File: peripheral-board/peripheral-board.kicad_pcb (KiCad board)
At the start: 2 copper layers, 165 x 100 mm, 248 parts, among them CON4001 BARREL_JACK, CON8001 SD_Card, J4001 53047-0510, J7001 FCR1295, J7002 53047-0310, P1001 Peripheral Bus, P1002 Power, Q4001 IRLML2244TRPbF, Q8001 BSS84LT1G, SW1001 Power, SW2001 1, SW2002 2, SW2003 3, SW2004 4, SW2005 5, SW2006 6, SW2007 7, SW2008 8, SW2009 9, SW2010 0, SW2011 +, SW2012 ´, SW2013 BKSP, SW2014 TROLL, SW2015 §, SW2016 UP, SW2017 RMB, SW2018 Q, SW2019 W, SW2020 E, SW2021 R, SW2022 T, SW2023 Y, SW2024 U, SW2025 I, SW2026 O, SW2027 P, SW2028 Å, SW2029 ¨, SW2030 RETURN, SW2031 ALT_GR, SW2032 <, SW2033 LEFT, SW2034 MMB, SW2035 A, SW2036 S, SW2037 D, SW2038 F, SW2039 G, SW2040 H, SW2041 J, SW2042 K, SW2043 L, SW2044 Ö, SW2045 Ä, SW2046 ', SW2047 ESC, SW2048 TAB, SW2049 ALT, SW2050 DOWN, SW2051 LMB, SW2052 SHIFT_L, SW2053 Z, SW2054 X, SW2055 C, SW2056 V, SW2057 B, SW2058 N, SW2059 M, SW2060 ,, SW2061 ., SW2062 -, SW2063 SHIFT_R, SW2064 FN_R, SW2065 SPACE, SW2066 FN_L, SW2067 RIGHT, SW2068 CTRL, SW2069 SPACE, U1001 ATTINY48-A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

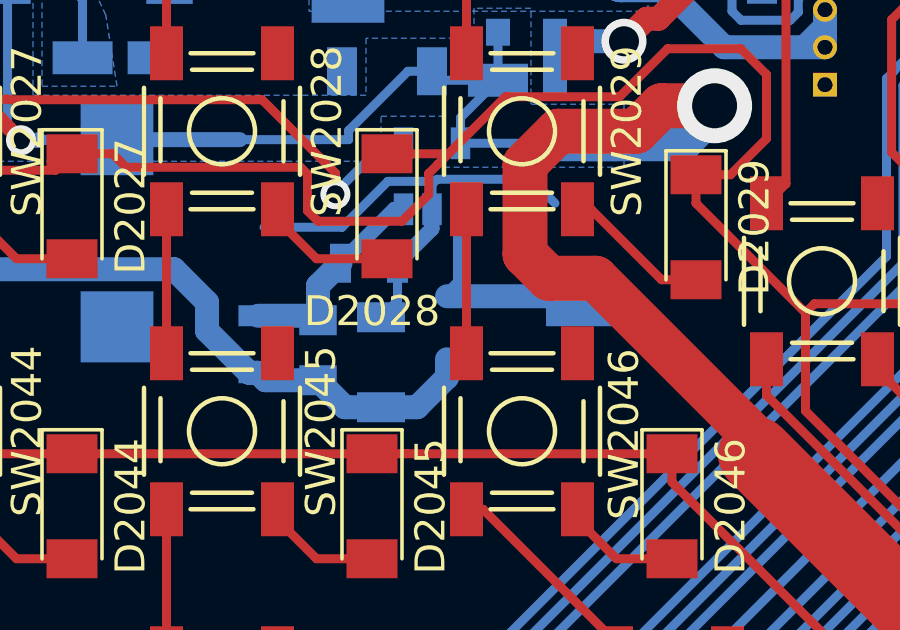
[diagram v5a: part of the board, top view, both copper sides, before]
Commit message: moved power supply capacitor to accomodate larger battery
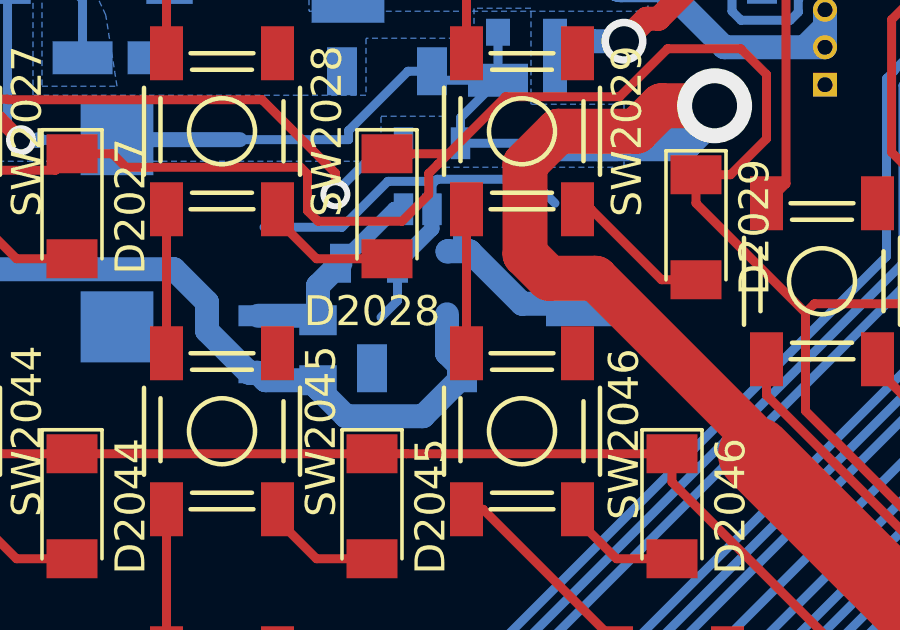
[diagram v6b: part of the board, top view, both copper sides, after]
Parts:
- moved D4007 1.50 mm to (215.0, 75.0)
- moved C4009 1.22 mm to (214.0, 77.9), turned to 180 degrees
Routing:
- net +24V: track 135.0 -> 137.7 mm
- net Net-(D4007-Pad2): track 7.69 -> 7.10 mm
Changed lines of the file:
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@@
     (thickness 1.6)
     (drawings 70)
-    (tracks 2229)
+    (tracks 2234)
     (zones 0)
     (modules 248)
@@
   )
   (setup
-    (last_trace_width 0.3)
+    (last_trace_width 0.5)
     (user_trace_width 0.25)
     (user_trace_width 0.4)
@@
   )
   (module Capacitors_SMD:C_1206 (layer B.Cu)
-    (at 212.8 77.7 90)
+    (at 214 77.9 180)
     (descr "Capacitor SMD 1206, reflow soldering, AVX (see smccp.pdf)")
     (tags "capacitor 1206")
     (attr smd)
-    (fp_text reference C4009 (at -13.3 -17.8 270) (layer B.SilkS)
+    (fp_text reference C4009 (at -13.3 -17.8) (layer B.SilkS)
       (effects (font (size 1 1) (thickness 0.15)) (justify mirror))
     )
-    (fp_text value 10u (at 0 -2.3 90) (layer B.Fab)
+    (fp_text value 10u (at 0 -2.3 180) (layer B.Fab)
       (effects (font (size 1 1) (thickness 0.15)) (justify mirror))
     )
@@
     (fp_line (start 1.6 -0.8) (end -1.6 -0.8) (layer B.Fab) (width 0.1))
     (fp_line (start -1.6 -0.8) (end -1.6 0.8) (layer B.Fab) (width 0.1))
-    (pad 2 smd rect (at 1.5 0 90) (size 1 1.6) (layers B.Cu B.Paste B.Mask)
+    (pad 2 smd rect (at 1.5 0 180) (size 1 1.6) (layers B.Cu B.Paste B.Mask)
       (net 69 GND))
-    (pad 1 smd rect (at -1.5 0 90) (size 1 1.6) (layers B.Cu B.Paste B.Mask)
+    (pad 1 smd rect (at -1.5 0 180) (size 1 1.6) (layers B.Cu B.Paste B.Mask)
       (net 101 +24V))
     (model Capacitors_SMD.3dshapes/C_1206.wrl
@@
   )
   (module Diodes_SMD:D_SOD-323 (layer B.Cu)
-    (at 215 76.55 90)
+    (at 215 75.05 90)
     (descr SOD-323)
     (tags SOD-323)
@@
   (segment (start 87.7824 136.5) (end 87.63 136.5) (width 0.3) (layer B.Cu) (net 100))
   (segment (start 178.98999 134.51001) (end 178.856986 134.51001) (width 0.3) (layer B.Cu) (net 100))
+  (segment (start 215 76.1) (end 215 77.4) (width 0.8) (layer B.Cu) (net 101))
+  (segment (start 215 77.4) (end 215.5 77.9) (width 0.8) (layer B.Cu) (net 101))
+  (segment (start 210.7 78.3) (end 210.7 78.570002) (width 0.8) (layer B.Cu) (net 101))
+  (segment (start 210.7 78.570002) (end 211.629998 79.5) (width 0.8) (layer B.Cu) (net 101))
+  (segment (start 211.629998 79.5) (end 214.2 79.5) (width 0.8) (layer B.Cu) (net 101))
+  (segment (start 214.2 79.5) (end 215.5 78.2) (width 0.8) (layer B.Cu) (net 101))
+  (segment (start 215.5 78.2) (end 215.5 77.9) (width 0.8) (layer B.Cu) (net 101))
   (segment (start 207 76.65) (end 208.4 78.05) (width 0.8) (layer B.Cu) (net 101))
   (segment (start 205.9 74.6) (end 207 75.7) (width 0.8) (layer B.Cu) (net 101))
@@
   (segment (start 96.586 77.6) (end 196.7 77.6) (width 0.8) (layer B.Cu) (net 101))
   (segment (start 196.7 77.6) (end 199.7 74.6) (width 0.8) (layer B.Cu) (net 101))
-  (segment (start 215 77.6) (end 215 78.2) (width 0.8) (layer B.Cu) (net 101))
-  (segment (start 215 78.2) (end 214 79.2) (width 0.8) (layer B.Cu) (net 101))
-  (segment (start 214 79.2) (end 212.8 79.2) (width 0.8) (layer B.Cu) (net 101))
   (segment (start 210.7 78.3) (end 208.95 78.3) (width 0.8) (layer B.Cu) (net 101))
   (segment (start 208.95 78.3) (end 208.7 78.05) (width 0.8) (layer B.Cu) (net 101))
-  (segment (start 212.8 79.2) (end 211.6 79.2) (width 0.8) (layer B.Cu) (net 101))
-  (segment (start 211.6 79.2) (end 210.7 78.3) (width 0.8) (layer B.Cu) (net 101))
   (segment (start 97 53.625) (end 98.857025 53.625) (width 0.3) (layer F.Cu) (net 102))
   (segment (start 98.857025 53.625) (end 99.132076 53.349949) (width 0.3) (layer F.Cu) (net 102))
@@
   (segment (start 208.7 76.15) (end 210.55 76.15) (width 0.8) (layer B.Cu) (net 123))
   (segment (start 210.55 76.15) (end 210.7 76.3) (width 0.8) (layer B.Cu) (net 123))
-  (segment (start 215 75.5) (end 219.25 75.5) (width 0.8) (layer B.Cu) (net 124))
+  (segment (start 215.45 72.6) (end 215.45 73.7) (width 0.5) (layer B.Cu) (net 124))
+  (segment (start 215.45 73.7) (end 215.75 74) (width 0.5) (layer B.Cu) (net 124))
+  (segment (start 219.5 75.75) (end 217.5 75.75) (width 0.8) (layer B.Cu) (net 124))
+  (segment (start 217.5 75.75) (end 215.75 74) (width 0.8) (layer B.Cu) (net 124))
+  (segment (start 215.75 74) (end 215.022806 74) (width 0.8) (layer B.Cu) (net 124))
+  (segment (start 215.022806 74) (end 215.011403 74.011403) (width 0.8) (layer B.Cu) (net 124))
   (segment (start 219.25 75.5) (end 219.5 75.75) (width 0.8) (layer B.Cu) (net 124))
-  (segment (start 215.45 72.6) (end 215.45 75.05) (width 0.5) (layer B.Cu) (net 124))
-  (segment (start 215.45 75.05) (end 215 75.5) (width 0.5) (layer B.Cu) (net 124))
   (segment (start 214.4 54.9) (end 214.4 62.05) (width 0.8) (layer B.Cu) (net 125))
   (segment (start 214.4 62.05) (end 215.25 62.9) (width 0.8) (layer B.Cu) (net 125))
@@
     (polygon
       (pts
-        (xy 237.5 148.9) (xy 237.5 148.9) (xy 186.5 148.9) (xy 237.5 148.9)
+        (xy 237.5 148.9) (xy 237.5 148.9) (xy 237.5 148.9)
       )
     )

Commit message: minor fixes to peripheral board
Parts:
- added R6001: 10k, Resistors_SMD:R_0805, F.Cu at (234.2, 105.0)
- added R6002: 10k, Resistors_SMD:R_0805, F.Cu at (240.2, 138.9)
- L4002: value 10u -> 8u2
- R4012: value 270k -> 220k
- R4013: value 13.3k -> 12k
- moved R7007 8.30 mm to (235.9, 138.8), turned to 180 degrees
- moved R7003 0.35 mm to (234.4, 108.0)
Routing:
- net Net-(R7007-Pad2): track 17.8 -> 5.10 mm
- net Net-(C7016-Pad1): track 7.02 -> 18.6 mm
- net +3V3: track 267.7 -> 276.4 mm
- net GND: track 291.5 -> 295.2 mm
- net Net-(C7009-Pad1): track 6.92 -> 9.72 mm

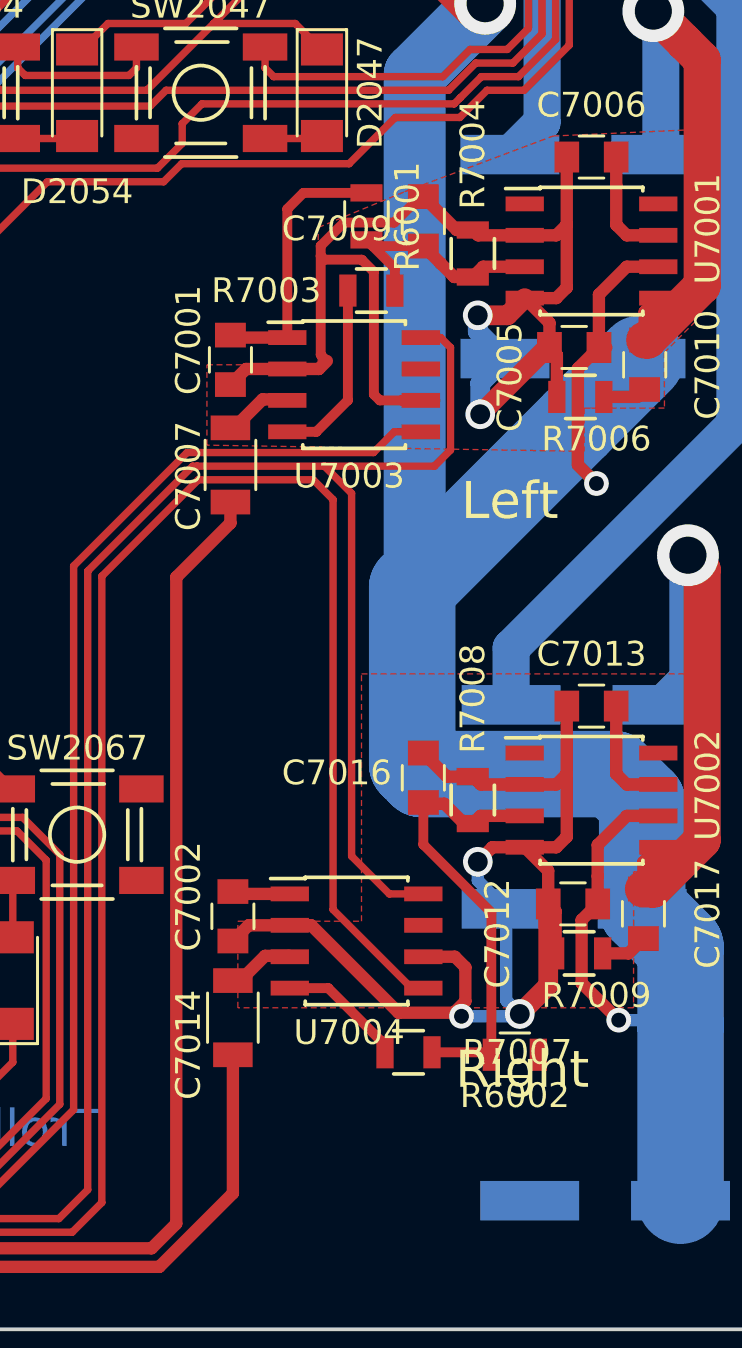
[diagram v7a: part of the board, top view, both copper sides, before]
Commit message: more audio circuit fixes
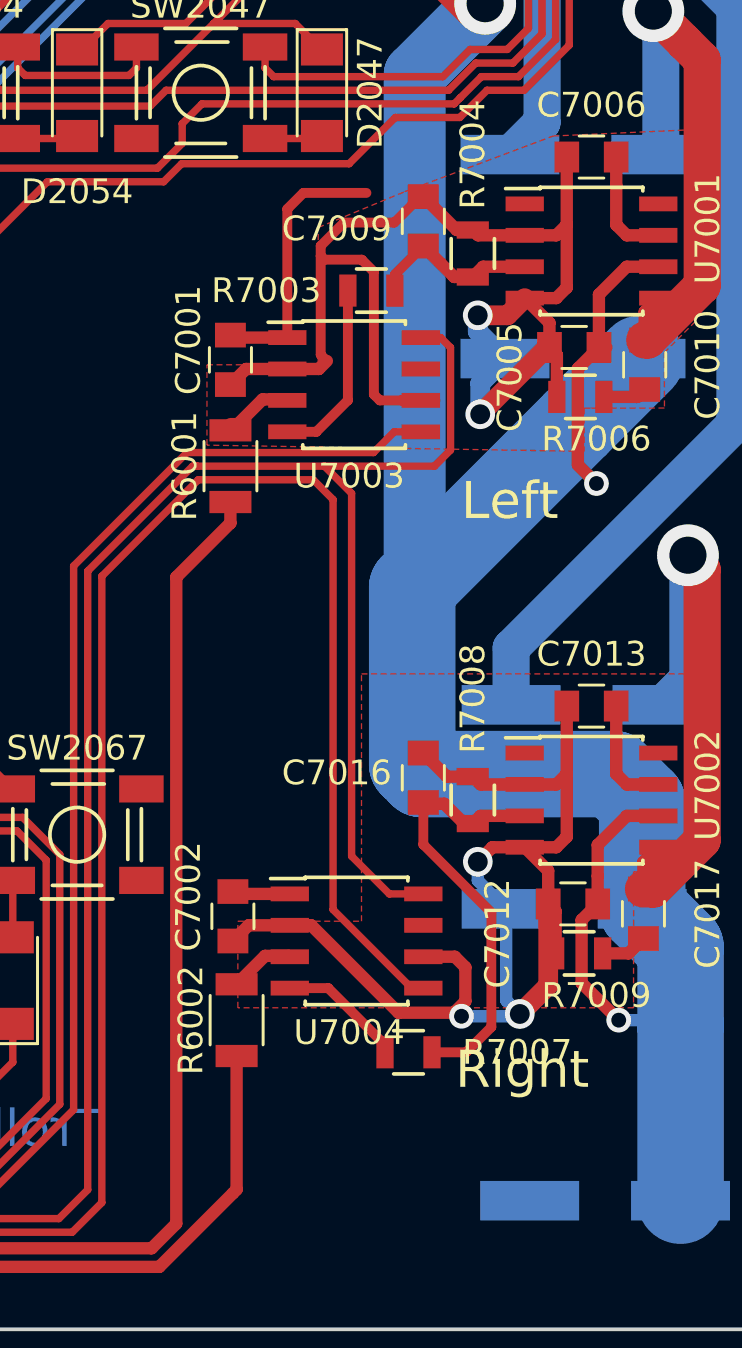
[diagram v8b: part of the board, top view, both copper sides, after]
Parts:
- removed C7007, C7014: 1u, Capacitors_SMD:C_1206
- R6001, R6002: value 10k -> 0; footprint Resistors_SMD:R_0805 -> Resistors_SMD:R_1206
- moved R6001 11.5 mm to (228.7, 115.1), turned to 90 degrees
- moved R6002 11.3 mm to (228.9, 137.5), turned to 90 degrees
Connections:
- R6001 pad 1: +3V3 -> /AUDIO_L
- R6001 pad 2: Net-(C7009-Pad1) -> Net-(R6001-Pad2)
- R6002 pad 1: +3V3 -> /AUDIO_R
- R6002 pad 2: Net-(C7016-Pad1) -> Net-(R6002-Pad2)
- U7003 pad 3: Net-(C7007-Pad1) -> Net-(R6001-Pad2)
- U7004 pad 3: Net-(C7014-Pad1) -> Net-(R6002-Pad2)
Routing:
- net Net-(R6001-Pad2): track 0.00 -> 10.4 mm
- net GND: track 295.2 -> 287.5 mm
- net Net-(C7007-Pad1): track 2.73 -> 0.00 mm
- net Net-(R6002-Pad2): track 0.00 -> 2.73 mm
- net Net-(C7014-Pad1): track 2.73 -> 0.00 mm
- net Net-(C7009-Pad1): track 9.72 -> 7.07 mm
- net Net-(C7016-Pad1): track 18.6 -> 17.9 mm
